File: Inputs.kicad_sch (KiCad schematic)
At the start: 0 parts

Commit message: began input/breakout changes
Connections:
- no-connect marks 0 -> 7
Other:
- note added: "4 buttons 4 switches"
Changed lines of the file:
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@@
 (kicad_sch (version 20230121) (generator eeschema)
   (paper "A4")
+  (no_connect (at 167.64 44.45))
+  (no_connect (at 193.04 44.45))
+  (no_connect (at 129.54 44.45))
+  (no_connect (at 142.24 44.45))
+  (no_connect (at 180.34 44.45))
+  (no_connect (at 116.84 44.45))
+  (no_connect (at 154.94 44.45))
+  (bus_entry (at 177.8 31.75) (size 2.54 2.54)
+    (stroke (width 0) (type default))
+  )
+  (bus_entry (at 203.2 31.75) (size 2.54 2.54)
+    (stroke (width 0) (type default))
+  )
+  (bus_entry (at 152.4 31.75) (size 2.54 2.54)
+    (stroke (width 0) (type default))
+  )
+  (bus_entry (at 139.7 31.75) (size 2.54 2.54)
+    (stroke (width 0) (type default))
+  )
+  (bus_entry (at 190.5 31.75) (size 2.54 2.54)
+    (stroke (width 0) (type default))
+  )
+  (bus_entry (at 127 31.75) (size 2.54 2.54)
+    (stroke (width 0) (type default))
+  )
+  (bus_entry (at 165.1 31.75) (size 2.54 2.54)
+    (stroke (width 0) (type default))
+  )
+  (wire (pts (xy 193.04 34.29) (xy 193.04 44.45))
+    (stroke (width 0) (type default))
+  )
+  (wire (pts (xy 142.24 34.29) (xy 142.24 44.45))
+    (stroke (width 0) (type default))
+  )
+  (wire (pts (xy 116.84 34.29) (xy 114.3 31.75))
+    (stroke (width 0) (type default))
+  )
+  (bus (pts (xy 203.2 31.75) (xy 209.55 31.75))
+    (stroke (width 0) (type default))
+  )
+  (bus (pts (xy 177.8 31.75) (xy 190.5 31.75))
+    (stroke (width 0) (type default))
+  )
+  (bus (pts (xy 165.1 31.75) (xy 177.8 31.75))
+    (stroke (width 0) (type default))
+  )
+  (wire (pts (xy 129.54 34.29) (xy 129.54 44.45))
+    (stroke (width 0) (type default))
+  )
+  (wire (pts (xy 167.64 34.29) (xy 167.64 44.45))
+    (stroke (width 0) (type default))
+  )
+  (bus (pts (xy 152.4 31.75) (xy 165.1 31.75))
+    (stroke (width 0) (type default))
+  )
+  (wire (pts (xy 154.94 34.29) (xy 154.94 44.45))
+    (stroke (width 0) (type default))
+  )
+  (bus (pts (xy 139.7 31.75) (xy 152.4 31.75))
+    (stroke (width 0) (type default))
+  )
+  (wire (pts (xy 205.74 34.29) (xy 205.74 44.45))
+    (stroke (width 0) (type default))
+  )
+  (wire (pts (xy 116.84 34.29) (xy 116.84 44.45))
+    (stroke (width 0) (type default))
+  )
+  (wire (pts (xy 180.34 34.29) (xy 180.34 44.45))
+    (stroke (width 0) (type default))
+  )
+  (bus (pts (xy 127 31.75) (xy 139.7 31.75))
+    (stroke (width 0) (type default))
+  )
+  (bus (pts (xy 190.5 31.75) (xy 203.2 31.75))
+    (stroke (width 0) (type default))
+  )
+  (text "4 buttons\n4 switches" (at 161.925 58.42 0)
+    (effects (font (size 1.27 1.27)) (justify left bottom))
+  )
+  (label "PD15" (at 116.84 34.29 270) (fields_autoplaced)
+    (effects (font (size 1.27 1.27)) (justify right bottom))
+  )
+  (label "PG8" (at 205.74 34.29 270) (fields_autoplaced)
+    (effects (font (size 1.27 1.27)) (justify right bottom))
+  )
+  (label "PG5" (at 167.64 34.29 270) (fields_autoplaced)
+    (effects (font (size 1.27 1.27)) (justify right bottom))
+  )
+  (label "PG6" (at 180.34 34.29 270) (fields_autoplaced)
+    (effects (font (size 1.27 1.27)) (justify right bottom))
+  )
+  (label "PG4" (at 154.94 34.29 270) (fields_autoplaced)
+    (effects (font (size 1.27 1.27)) (justify right bottom))
+  )
+  (label "PG2" (at 129.54 34.29 270) (fields_autoplaced)
+    (effects (font (size 1.27 1.27)) (justify right bottom))
+  )
+  (label "PG7" (at 193.04 34.29 270) (fields_autoplaced)
+    (effects (font (size 1.27 1.27)) (justify right bottom))
+  )
+  (label "PG3" (at 142.24 34.29 270) (fields_autoplaced)
+    (effects (font (size 1.27 1.27)) (justify right bottom))
+  )
+  (hierarchical_label "PG[2..8]" (shape input) (at 209.55 31.75 0) (fields_autoplaced)
+    (effects (font (size 1.27 1.27)) (justify left))
+  )
+  (hierarchical_label "PD15" (shape input) (at 114.3 31.75 180) (fields_autoplaced)
+    (effects (font (size 1.27 1.27)) (justify right))
+  )
 )

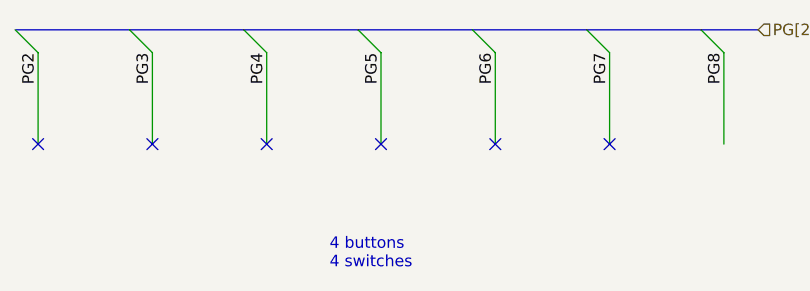
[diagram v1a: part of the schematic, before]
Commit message: new bt module + preliminary reverse protection
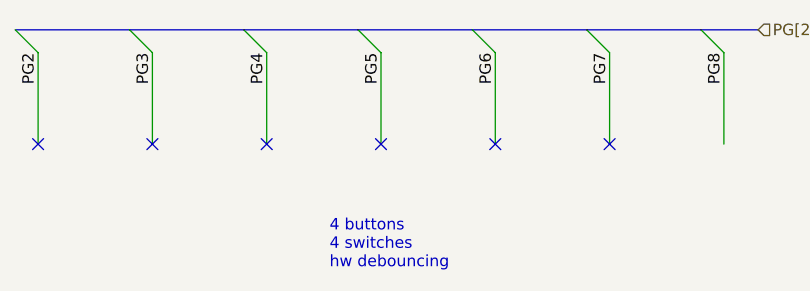
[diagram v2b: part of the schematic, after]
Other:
- note added: "4 buttons 4 switches hw debouncing"
- note removed: "4 buttons 4 switches"
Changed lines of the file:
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@@
     (stroke (width 0) (type default))
   )
-  (text "4 buttons\n4 switches" (at 161.925 58.42 0)
+  (text "4 buttons\n4 switches\nhw debouncing" (at 161.925 58.42 0)
     (effects (font (size 1.27 1.27)) (justify left bottom))
   )

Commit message: basic inputs
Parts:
- added C52, C53, C54, C55, C56, C57, C58, C59: .1u, symbol Device:C
- added R33, R43, R44, R45, R46, R47, R48, R49: 1k, symbol Device:R
- added SW10, SW11, SW8, SW9: SW_SPST, symbol Switch:SW_SPST
- added SW4, SW5, SW6, SW7: SW_Push, symbol Switch:SW_Push
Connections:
- net PD15: now also C52.1, R33.1
- net PG2: now also C53.1, R43.1
- net PG3: now also C54.1, R44.1
- net PG4: now also C55.1, R45.1
- net PG5: now also C56.1, R46.1
- net PG6: now also C57.1, R47.1
- net PG7: now also C58.1, R48.1
- net PG8: now also C59.1, R49.1
- new net: R48.2, SW10.2 (B)
- new net: R46.2, SW8.2 (B)
- new net: R44.2, SW6.2
- new net: R49.2, SW11.2 (B)
- new net: R45.2, SW7.2
- new net: R33.2, SW4.2
- new net: R47.2, SW9.2 (B)
- new net: R43.2, SW5.2
- new net GND: C52.2, C53.2, C54.2, C55.2, C56.2, C57.2, C58.2, C59.2, SW10.1 (A), SW11.1 (A), SW4.1, SW5.1, SW6.1, SW7.1, SW8.1 (A), SW9.1 (A)
- no-connect marks 7 -> 0
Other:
- note added: "*must enable internal pullup resistor (~40k)"
- note added: "4 buttons 4 switches hw debouncing (8ms bounce time)"
- note added: "Inputs"
- note removed: "4 buttons 4 switches hw debouncing"

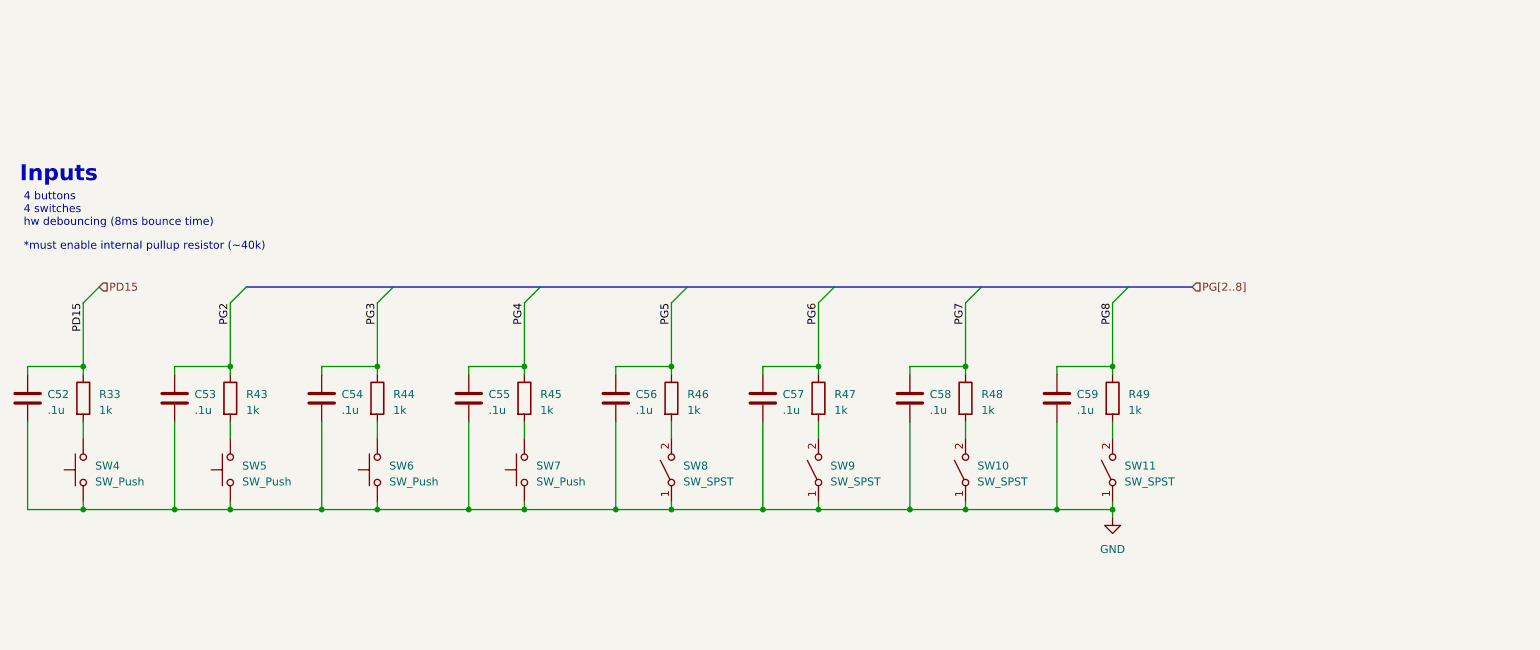
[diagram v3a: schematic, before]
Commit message: switch changes, some caps, annotations
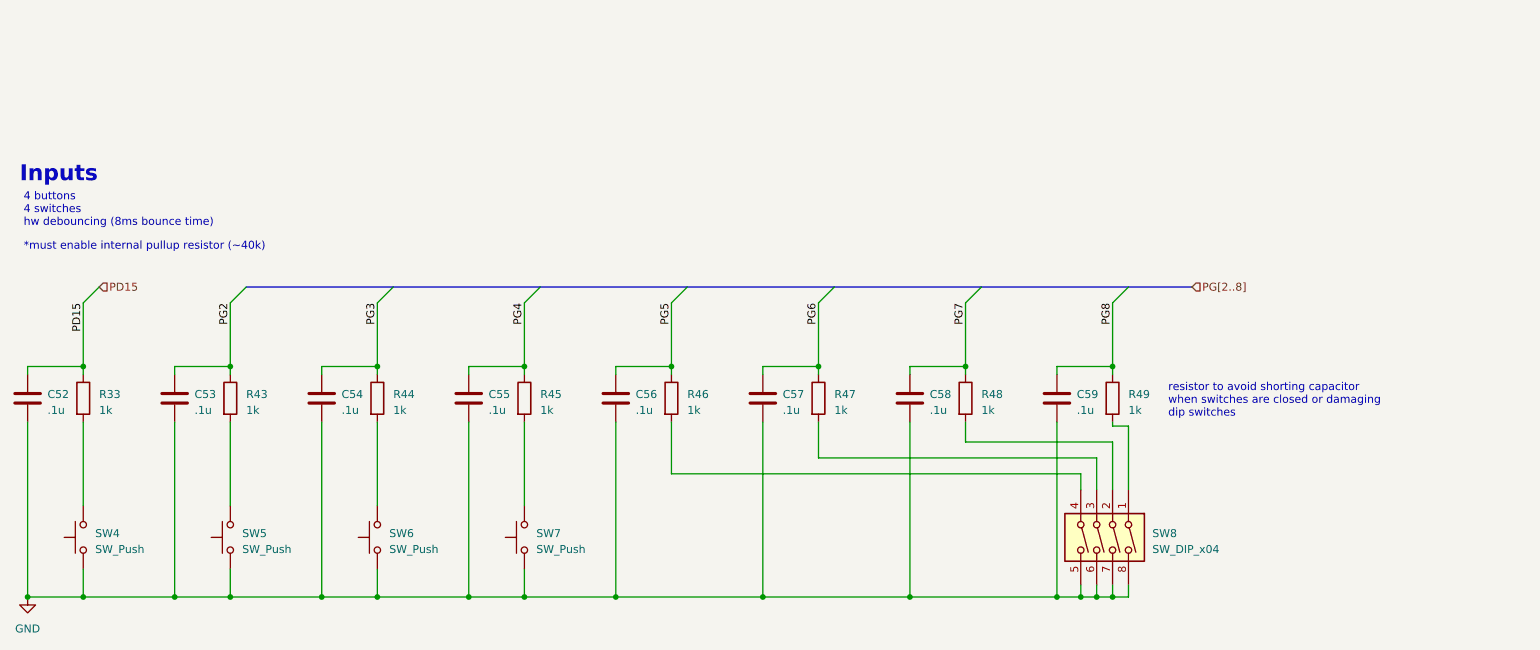
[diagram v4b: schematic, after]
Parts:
- removed SW10, SW11, SW9: SW_SPST, symbol Switch:SW_SPST
- SW4, SW5, SW6, SW7: footprint (none) -> UTSVT_Special:SW_SPST_B3SL-1002P
- SW8: value SW_SPST -> SW_DIP_x04; symbol Switch:SW_SPST -> Switch:SW_DIP_x04; P/N (none) -> DS04-254-1-04BK-SMT
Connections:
- net GND: now also SW8.5, SW8.6, SW8.7, SW8.8; no longer SW8.1 (A)
- net at R48.2: now also SW8.2
- net at R46.2: now also SW8.4; no longer SW8.2 (B)
- net at R49.2: now also SW8.1
- net at R47.2: now also SW8.3
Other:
- note added: "resistor to avoid shorting capacitor when switches are closed or damaging dip switches"
- moved on the sheet: SW4, SW5, SW6, SW7

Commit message: layout rearranging
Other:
- note added: "REMOVE RESISTOR"
- note removed: "resistor to avoid shorting capacitor when switches are closed or damaging dip switches"
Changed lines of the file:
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@@
     (effects (font (size 2.54 2.54) (thickness 0.508) bold) (justify left bottom))
   )
-  (text "resistor to avoid shorting capacitor\nwhen switches are closed or damaging\ndip switches"
-    (at 237.49 95.25 0)
+  (text "REMOVE RESISTOR" (at 237.49 95.25 0)
     (effects (font (size 1.27 1.27)) (justify left bottom))
   )

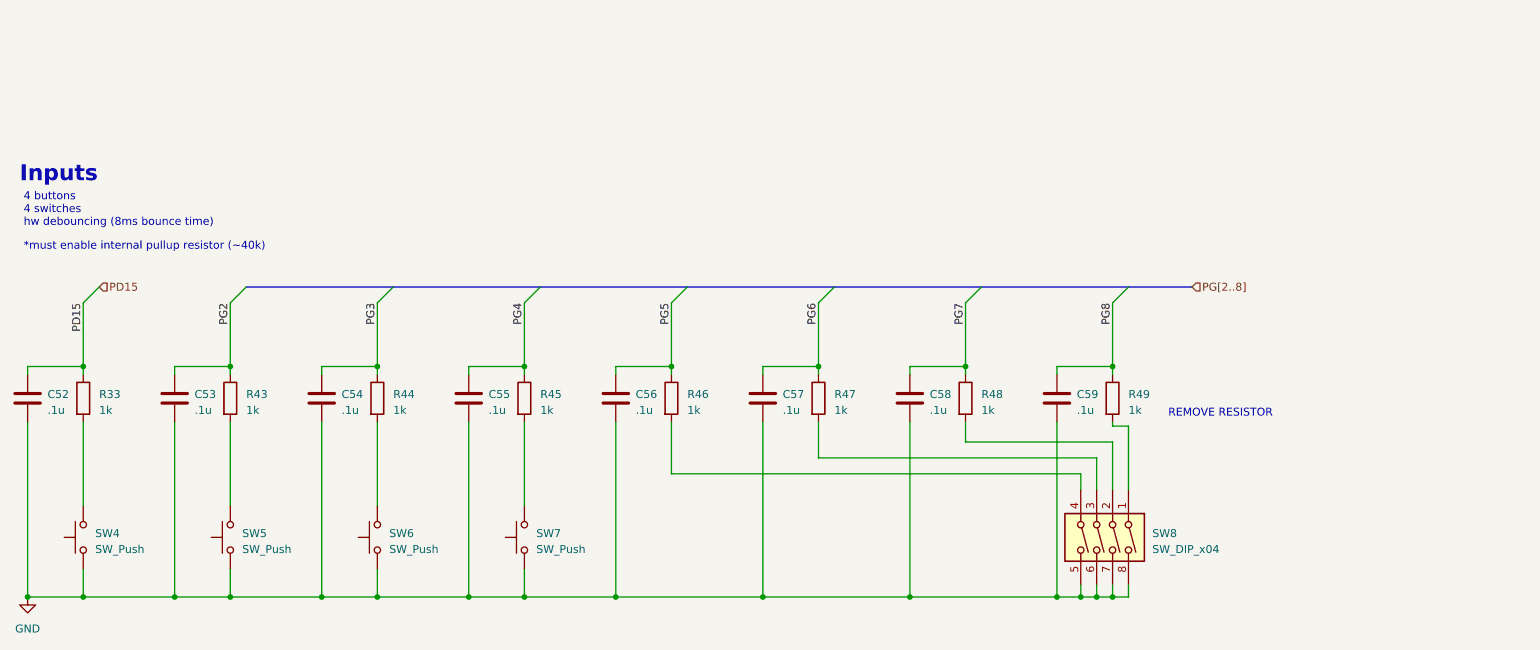
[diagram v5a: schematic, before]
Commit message: inputs routing + fixed models + clock keepouts
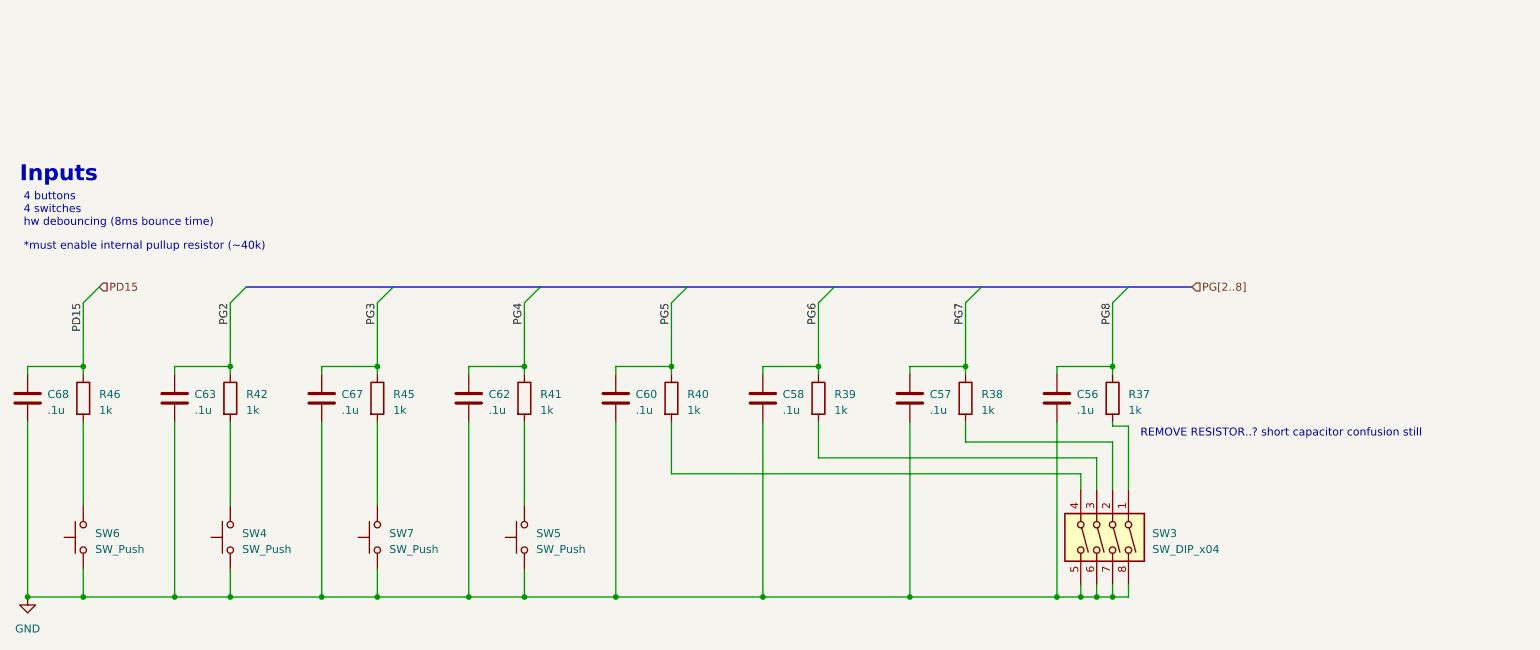
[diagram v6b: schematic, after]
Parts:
- C56: renamed from C59; footprint (none) -> Capacitor_SMD:C_0805_2012Metric; P/N (none) -> 0805YC106KAT2A
- C57: renamed from C58; footprint (none) -> Capacitor_SMD:C_0805_2012Metric; P/N (none) -> 0805YC106KAT2A
- C58: renamed from C57; footprint (none) -> Capacitor_SMD:C_0805_2012Metric; P/N (none) -> 0805YC106KAT2A
- C60: renamed from C56; footprint (none) -> Capacitor_SMD:C_0805_2012Metric; P/N (none) -> 0805YC106KAT2A
- C62: renamed from C55; footprint (none) -> Capacitor_SMD:C_0805_2012Metric; P/N (none) -> 0805YC106KAT2A
- C63: renamed from C53; footprint (none) -> Capacitor_SMD:C_0805_2012Metric; P/N (none) -> 0805YC106KAT2A
- C67: renamed from C54; footprint (none) -> Capacitor_SMD:C_0805_2012Metric; P/N (none) -> 0805YC106KAT2A
- C68: renamed from C52; footprint (none) -> Capacitor_SMD:C_0805_2012Metric; P/N (none) -> 0805YC106KAT2A
- R37: renamed from R49; footprint (none) -> Resistor_SMD:R_0805_2012Metric; P/N (none) -> CRCW08051K00FKEA
- R38: renamed from R48; footprint (none) -> Resistor_SMD:R_0805_2012Metric; P/N (none) -> CRCW08051K00FKEA
- R39: renamed from R47; footprint (none) -> Resistor_SMD:R_0805_2012Metric; P/N (none) -> CRCW08051K00FKEA
- R40: renamed from R46; footprint (none) -> Resistor_SMD:R_0805_2012Metric; P/N (none) -> CRCW08051K00FKEA
- R41: renamed from R45; footprint (none) -> Resistor_SMD:R_0805_2012Metric; P/N (none) -> CRCW08051K00FKEA
- R42: renamed from R43; footprint (none) -> Resistor_SMD:R_0805_2012Metric; P/N (none) -> CRCW08051K00FKEA
- R45: renamed from R44; footprint (none) -> Resistor_SMD:R_0805_2012Metric; P/N (none) -> CRCW08051K00FKEA
- R46: renamed from R33; footprint (none) -> Resistor_SMD:R_0805_2012Metric; P/N (none) -> CRCW08051K00FKEA
- SW3: renamed from SW8; footprint (none) -> Button_Switch_SMD:SW_DIP_SPSTx04_Slide_6.7x11.72mm_W8.61mm_P2.54mm_LowProfile; P/N DS04-254-1-04BK-SMT -> 219-4LPST
- SW4: renamed from SW5; P/N (none) -> EVQ-7Q203W or B3SL-1002P
- SW5: renamed from SW7; P/N (none) -> EVQ-7Q203W or B3SL-1002P
- SW6: renamed from SW4; P/N (none) -> EVQ-7Q203W or B3SL-1002P
- SW7: renamed from SW6; P/N (none) -> EVQ-7Q203W or B3SL-1002P
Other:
- note added: "REMOVE RESISTOR..? short capacitor confusion still"
- note removed: "REMOVE RESISTOR"
